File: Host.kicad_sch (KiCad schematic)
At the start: 15 parts, among them J2 UJ2-MBH-1-SMT-TR, U2 MPM3612-33, U3 STM32G061GxUx

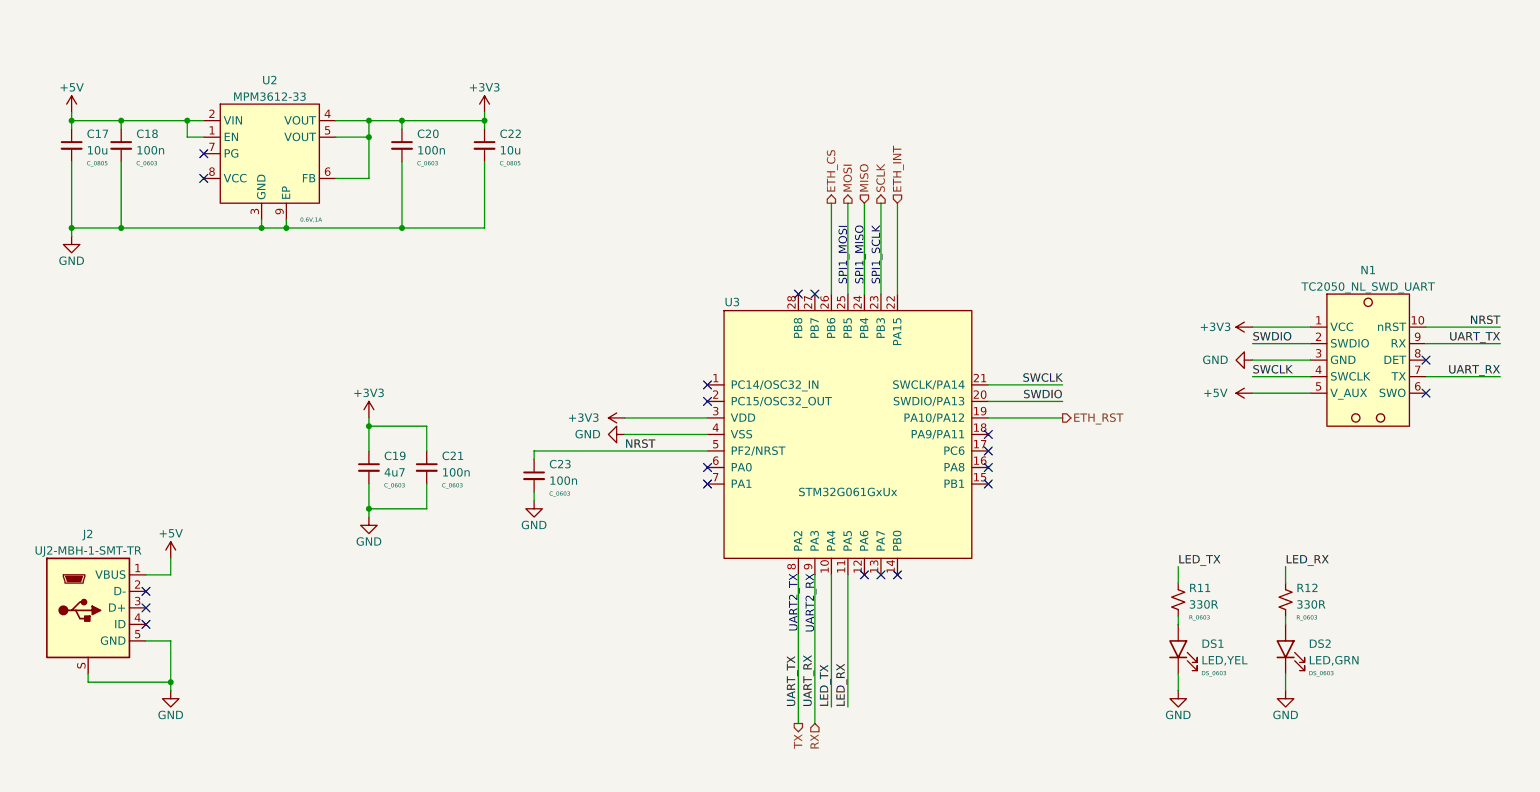
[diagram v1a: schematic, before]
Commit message: Add in RS232
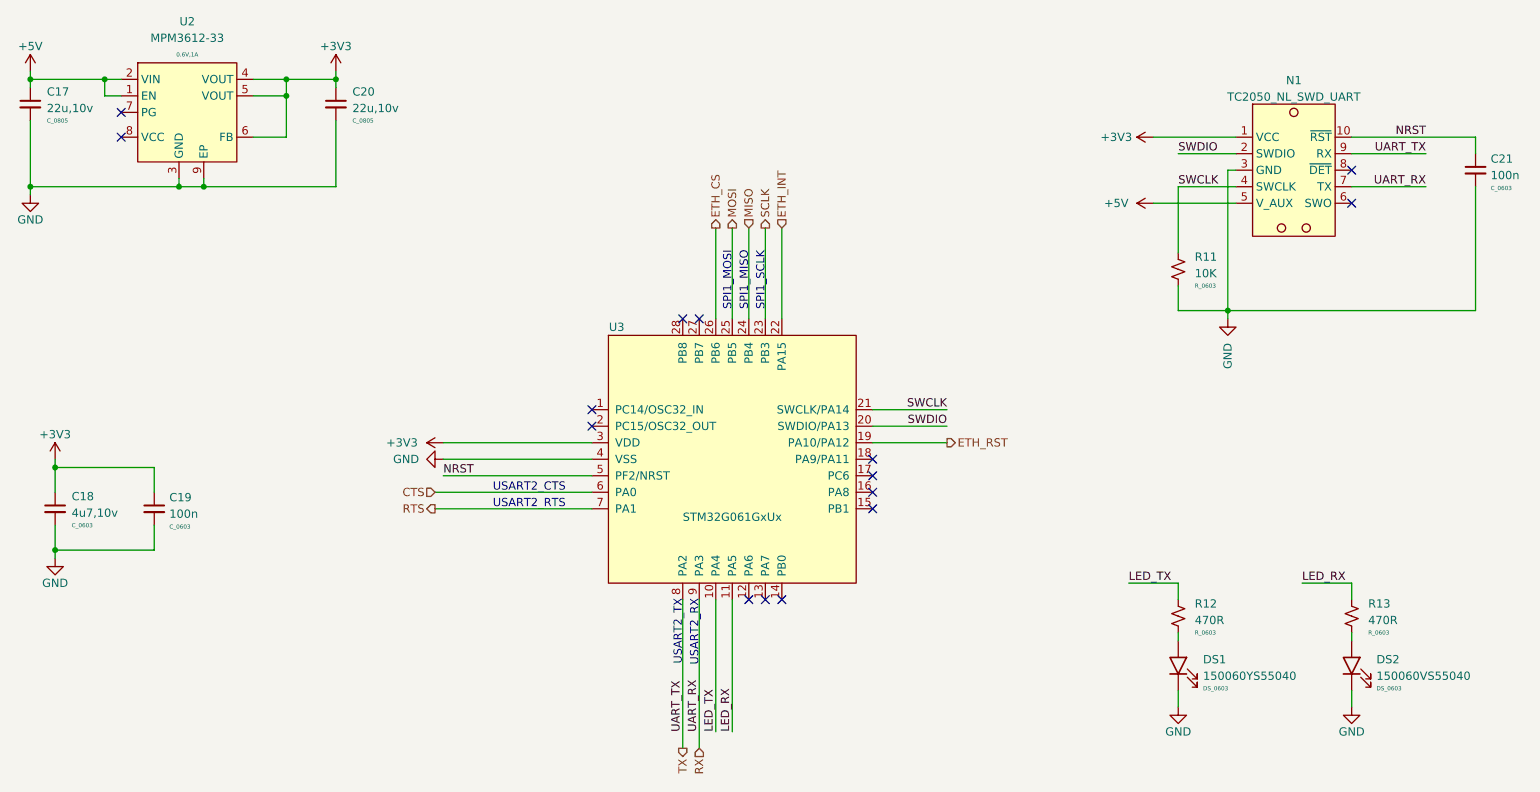
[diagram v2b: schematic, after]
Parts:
- removed C18, C20, C23: 100n, C_Capacitor:C_0603, symbol C_Capacitor:C_0603
- removed C22: 10u, C_Capacitor:C_0805, symbol C_Capacitor:C_0805
- removed DS1: LED,YEL, DS_LED:DS_0603, symbol DS_LED:DS_0603
- removed DS2: LED,GRN, DS_LED:DS_0603, symbol DS_LED:DS_0603
- removed J2: UJ2-MBH-1-SMT-TR, J_Connector:USB_Mini_SMD_Horizontal, symbol J_Connector:UJ2-MBH-1-SMT-TR
- removed U2: MPM3612-33, U_IC:LGA8_3x3_EP_MPM, symbol U_Power:MPM3612
- added C20: 22u,10v, C_Capacitor:C_0805, symbol C_Capacitor:C_0805
- added C21: 100n, C_Capacitor:C_0603, symbol C_Capacitor:C_0603
- added DS1: 150060YS55040, DS_LED:DS_0603, symbol DS_LED:150060YS55040
- added DS2: 150060VS55040, DS_LED:DS_0603, symbol DS_LED:150060VS55040
- added R11: 10K, R_Resistor:R_0603, symbol R_Resistor:R_0603
- added U2: MPM3612-33, U_IC:LGA8_3x3_EP_MPM, symbol U_PowerSwitching:MPM3612
- C17: value 10u -> 22u,10v
- C18: renamed from C19; value 4u7 -> 4u7,10v
- R12: renamed from R11; value 330R -> 470R
- R13: renamed from R12; value 330R -> 470R
- renumbered C21 to C19
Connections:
- net +3V3: now also C20.1, U2.4 (VOUT), U2.5 (VOUT), U2.6 (FB)
- net +5V: now also U2.1 (EN), U2.2 (VIN)
- net GND: now also C20.2, C21.2, DS1.1 (K), DS2.1 (K), R11.2, U2.3 (GND), U2.9 (EP)
- net NRST: now also C21.1
- net SWCLK: now also R11.1
- net CTS: now reaches U3.6 (PA0)
- net RTS: now reaches U3.7 (PA1)
- net at R13.2: now also DS2.2 (A)
- net at R12.2: now also DS1.2 (A)
- no-connect marks 20 -> 15
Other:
- note added: "USART2_CTS"
- note added: "USART2_RTS"
- note added: "USART2_RX"
- note added: "USART2_TX"
- note removed: "UART2_RX"
- note removed: "UART2_TX"
- company: TL Embedded Ltd -> TL Embedded
- moved on the sheet: C18, C19, N1, R12, R13, U3
